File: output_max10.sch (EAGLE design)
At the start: 59 parts, among them IC4 IS61WV1288EEBLL-10HLI, IC5 10M04EQFP144, Q1 25MHz

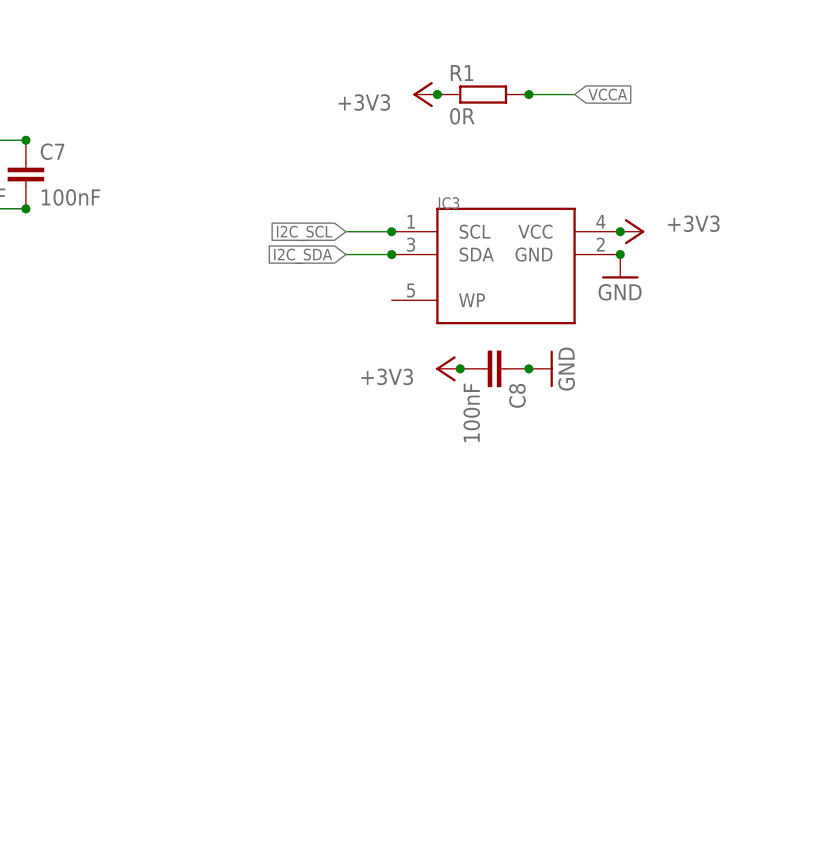
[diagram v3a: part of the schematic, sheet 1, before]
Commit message: clean up board some more; change eeprom to SOIC
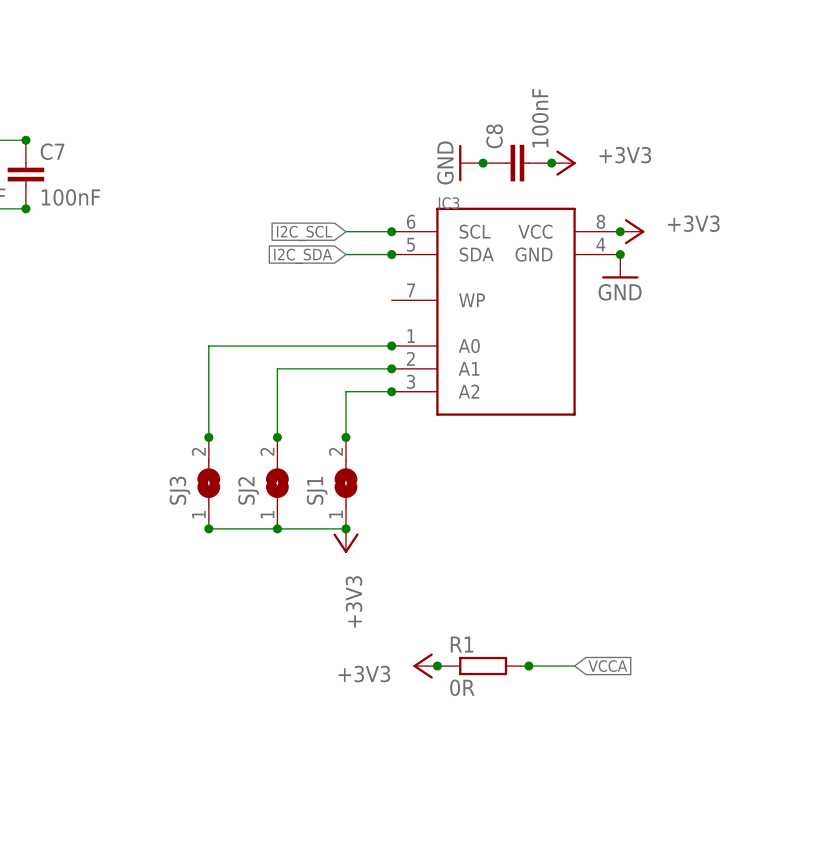
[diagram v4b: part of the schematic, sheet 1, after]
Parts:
- added SJ1, SJ2, SJ3: (no value), jumper:SJ
- IC3: device lichtenstein_onion:AT24C02D -> lichtenstein_onion:AT24C02DSOIC-8
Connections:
- new net N$5: IC3.A2, SJ1.2
- new net N$6: IC3.A1, SJ2.2
- new net N$7: IC3.A0, SJ3.2
- net +3V3: now also SJ1.1, SJ2.1, SJ3.1
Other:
- moved on the sheet: C8, R1
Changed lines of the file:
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@@
 <attribute name="MOUSER" value="710-885012207072"/>
 </part>
-<part name="IC3" library="lichtenstein_onion" deviceset="AT24C02D" device=""/>
 <part name="C8" library="rcl" library_urn="urn:adsk.eagle:library:334" deviceset="C-EU" device="C0805" package3d_urn="urn:adsk.eagle:package:23617/2" value="100nF">
 <attribute name="MOUSER" value="710-885012207072"/>
@@
 <part name="GND23" library="supply1" library_urn="urn:adsk.eagle:library:371" deviceset="GND" device=""/>
 <part name="+3V6" library="supply1" library_urn="urn:adsk.eagle:library:371" deviceset="+3V3" device=""/>
+<part name="IC3" library="lichtenstein_onion" deviceset="AT24C02D" device="SOIC-8"/>
+<part name="SJ1" library="jumper" library_urn="urn:adsk.eagle:library:252" deviceset="SJ" device="" package3d_urn="urn:adsk.eagle:package:15471/1"/>
+<part name="SJ2" library="jumper" library_urn="urn:adsk.eagle:library:252" deviceset="SJ" device="" package3d_urn="urn:adsk.eagle:package:15471/1"/>
+<part name="SJ3" library="jumper" library_urn="urn:adsk.eagle:library:252" deviceset="SJ" device="" package3d_urn="urn:adsk.eagle:package:15471/1"/>
+<part name="+3V7" library="supply1" library_urn="urn:adsk.eagle:library:371" deviceset="+3V3" device=""/>
 </parts>
 <sheets>
@@
 <attribute name="MOUSER" x="53.34" y="167.64" size="1.27" layer="96" display="off"/>
 </instance>
-<instance part="R1" gate="G$1" x="114.3" y="175.26">
-<attribute name="MOUSER" x="114.3" y="175.26" size="1.27" layer="96" align="top-center" display="off"/>
-</instance>
-<instance part="+3V36" gate="G$1" x="106.68" y="175.26" smashed="yes" rot="R90">
-<attribute name="VALUE" x="104.14" y="175.26" size="1.778" layer="96" rot="R180"/>
-</instance>
-<instance part="IC3" gate="G$1" x="109.22" y="162.56"/>
-<instance part="C8" gate="G$1" x="116.84" y="144.78" rot="R270">
-<attribute name="MOUSER" x="116.84" y="144.78" size="1.27" layer="96" rot="R270" align="top-center" display="off"/>
-</instance>
-<instance part="GND9" gate="1" x="121.92" y="144.78" rot="R90"/>
-<instance part="+3V37" gate="G$1" x="109.22" y="144.78" smashed="yes" rot="R90">
-<attribute name="VALUE" x="106.68" y="144.78" size="1.778" layer="96" rot="R180"/>
+<instance part="R1" gate="G$1" x="114.3" y="111.76">
+<attribute name="MOUSER" x="114.3" y="111.76" size="1.27" layer="96" align="top-center" display="off"/>
+</instance>
+<instance part="+3V36" gate="G$1" x="106.68" y="111.76" smashed="yes" rot="R90">
+<attribute name="VALUE" x="104.14" y="111.76" size="1.778" layer="96" rot="R180"/>
+</instance>
+<instance part="C8" gate="G$1" x="116.84" y="167.64" rot="R90">
+<attribute name="MOUSER" x="116.84" y="167.64" size="1.27" layer="96" rot="R90" align="top-center" display="off"/>
+</instance>
+<instance part="GND9" gate="1" x="111.76" y="167.64" rot="R270"/>
+<instance part="+3V37" gate="G$1" x="124.46" y="167.64" smashed="yes" rot="R270">
+<attribute name="VALUE" x="127" y="167.64" size="1.778" layer="96"/>
 </instance>
 <instance part="+3V38" gate="G$1" x="132.08" y="160.02" smashed="yes" rot="R270">
@@
 <instance part="H3" gate="G$1" x="121.92" y="12.7"/>
 <instance part="H4" gate="G$1" x="121.92" y="5.08"/>
+<instance part="IC3" gate="G$1" x="109.22" y="162.56"/>
+<instance part="SJ1" gate="1" x="99.06" y="132.08" rot="R90"/>
+<instance part="SJ2" gate="1" x="91.44" y="132.08" rot="R90"/>
+<instance part="SJ3" gate="1" x="83.82" y="132.08" rot="R90"/>
+<instance part="+3V7" gate="G$1" x="99.06" y="124.46" smashed="yes" rot="R180">
+<attribute name="VALUE" x="99.06" y="121.92" size="1.778" layer="96" rot="R270"/>
+</instance>
 </instances>
 <busses>
@@
 <pinref part="R1" gate="G$1" pin="1"/>
 <pinref part="+3V36" gate="G$1" pin="+3V3"/>
-<junction x="109.22" y="175.26"/>
+<junction x="109.22" y="111.76"/>
 </segment>
 <segment>
 <pinref part="C8" gate="G$1" pin="2"/>
 <pinref part="+3V37" gate="G$1" pin="+3V3"/>
-<junction x="111.76" y="144.78"/>
-</segment>
-<segment>
+<junction x="121.92" y="167.64"/>
+</segment>
+<segment>
+<pinref part="+3V38" gate="G$1" pin="+3V3"/>
 <pinref part="IC3" gate="G$1" pin="VCC"/>
-<pinref part="+3V38" gate="G$1" pin="+3V3"/>
 <junction x="129.54" y="160.02"/>
+</segment>
+<segment>
+<pinref part="SJ3" gate="1" pin="1"/>
+<pinref part="SJ1" gate="1" pin="1"/>
+<wire x1="83.82" y1="127" x2="91.44" y2="127" width="0.1524" layer="91"/>
+<pinref part="+3V7" gate="G$1" pin="+3V3"/>
+<junction x="99.06" y="127"/>
+<pinref part="SJ2" gate="1" pin="1"/>
+<junction x="91.44" y="127"/>
+<wire x1="91.44" y1="127" x2="99.06" y2="127" width="0.1524" layer="91"/>
+<junction x="83.82" y="127"/>
 </segment>
 </net>
@@
 <pinref part="C8" gate="G$1" pin="1"/>
 <pinref part="GND9" gate="1" pin="GND"/>
-<junction x="119.38" y="144.78"/>
-</segment>
-<segment>
+<junction x="114.3" y="167.64"/>
+</segment>
+<segment>
+<pinref part="GND10" gate="1" pin="GND"/>
 <pinref part="IC3" gate="G$1" pin="GND"/>
-<pinref part="GND10" gate="1" pin="GND"/>
 <junction x="129.54" y="157.48"/>
 </segment>
@@
 </segment>
 <segment>
-<pinref part="IC3" gate="G$1" pin="SCL"/>
 <wire x1="104.14" y1="160.02" x2="99.06" y2="160.02" width="0.1524" layer="91"/>
 <label x="99.06" y="160.02" size="1.27" layer="95" rot="R180" xref="yes"/>
+<pinref part="IC3" gate="G$1" pin="SCL"/>
 <junction x="104.14" y="160.02"/>
 </segment>
@@
 </segment>
 <segment>
-<pinref part="IC3" gate="G$1" pin="SDA"/>
 <wire x1="104.14" y1="157.48" x2="99.06" y2="157.48" width="0.1524" layer="91"/>
 <label x="99.06" y="157.48" size="1.27" layer="95" rot="R180" xref="yes"/>
+<pinref part="IC3" gate="G$1" pin="SDA"/>
 <junction x="104.14" y="157.48"/>
 </segment>
@@
 <segment>
 <pinref part="R1" gate="G$1" pin="2"/>
-<wire x1="119.38" y1="175.26" x2="124.46" y2="175.26" width="0.1524" layer="91"/>
-<label x="124.46" y="175.26" size="1.27" layer="95" xref="yes"/>
-<junction x="119.38" y="175.26"/>
+<wire x1="119.38" y1="111.76" x2="124.46" y2="111.76" width="0.1524" layer="91"/>
+<label x="124.46" y="111.76" size="1.27" layer="95" xref="yes"/>
+<junction x="119.38" y="111.76"/>
 </segment>
 </net>
@@
 </segment>
 </net>
+<net name="N$5" class="0">
+<segment>
+<pinref part="SJ1" gate="1" pin="2"/>
+<pinref part="IC3" gate="G$1" pin="A2"/>
+<wire x1="99.06" y1="137.16" x2="99.06" y2="142.24" width="0.1524" layer="91"/>
+<wire x1="99.06" y1="142.24" x2="104.14" y2="142.24" width="0.1524" layer="91"/>
+<junction x="99.06" y="137.16"/>
+<junction x="104.14" y="142.24"/>
+</segment>
+</net>
+<net name="N$6" class="0">
+<segment>
+<pinref part="IC3" gate="G$1" pin="A1"/>
+<pinref part="SJ2" gate="1" pin="2"/>
+<wire x1="104.14" y1="144.78" x2="91.44" y2="144.78" width="0.1524" layer="91"/>
+<wire x1="91.44" y1="144.78" x2="91.44" y2="137.16" width="0.1524" layer="91"/>
+<junction x="91.44" y="137.16"/>
+<junction x="104.14" y="144.78"/>
+</segment>
+</net>
+<net name="N$7" class="0">
+<segment>
+<pinref part="SJ3" gate="1" pin="2"/>
+<pinref part="IC3" gate="G$1" pin="A0"/>
+<wire x1="83.82" y1="137.16" x2="83.82" y2="147.32" width="0.1524" layer="91"/>
+<wire x1="83.82" y1="147.32" x2="104.14" y2="147.32" width="0.1524" layer="91"/>
+<junction x="83.82" y="137.16"/>
+<junction x="104.14" y="147.32"/>
+</segment>
+</net>

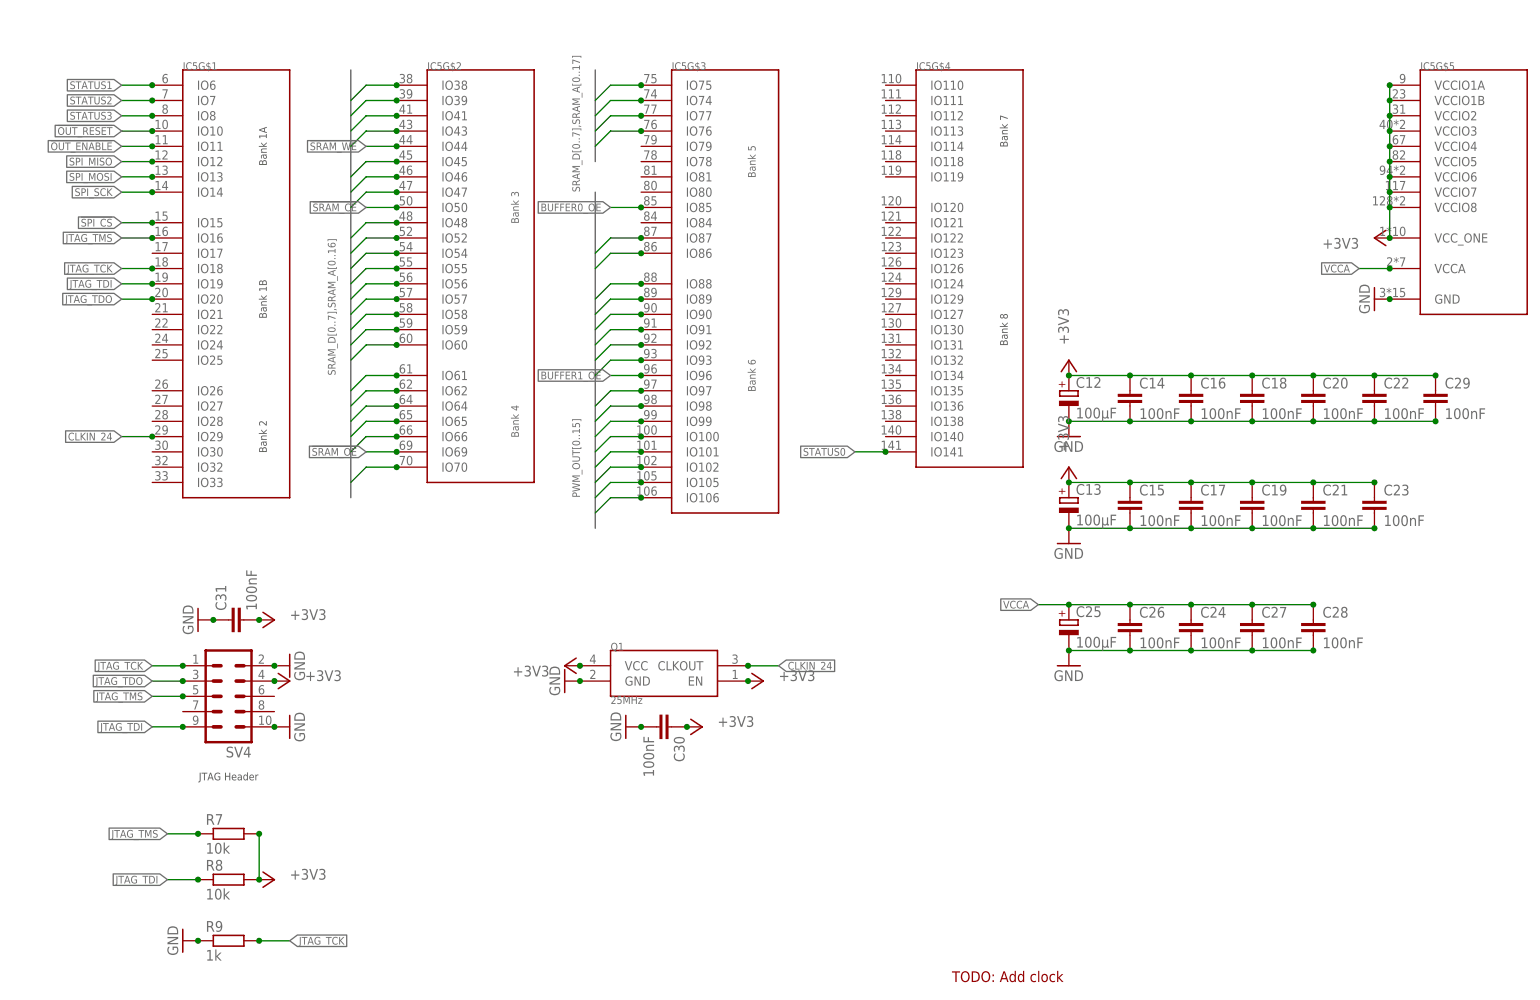
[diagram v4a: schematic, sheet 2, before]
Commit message: Fixed bulk capacitor footprints; made +V for output channels independent on output board
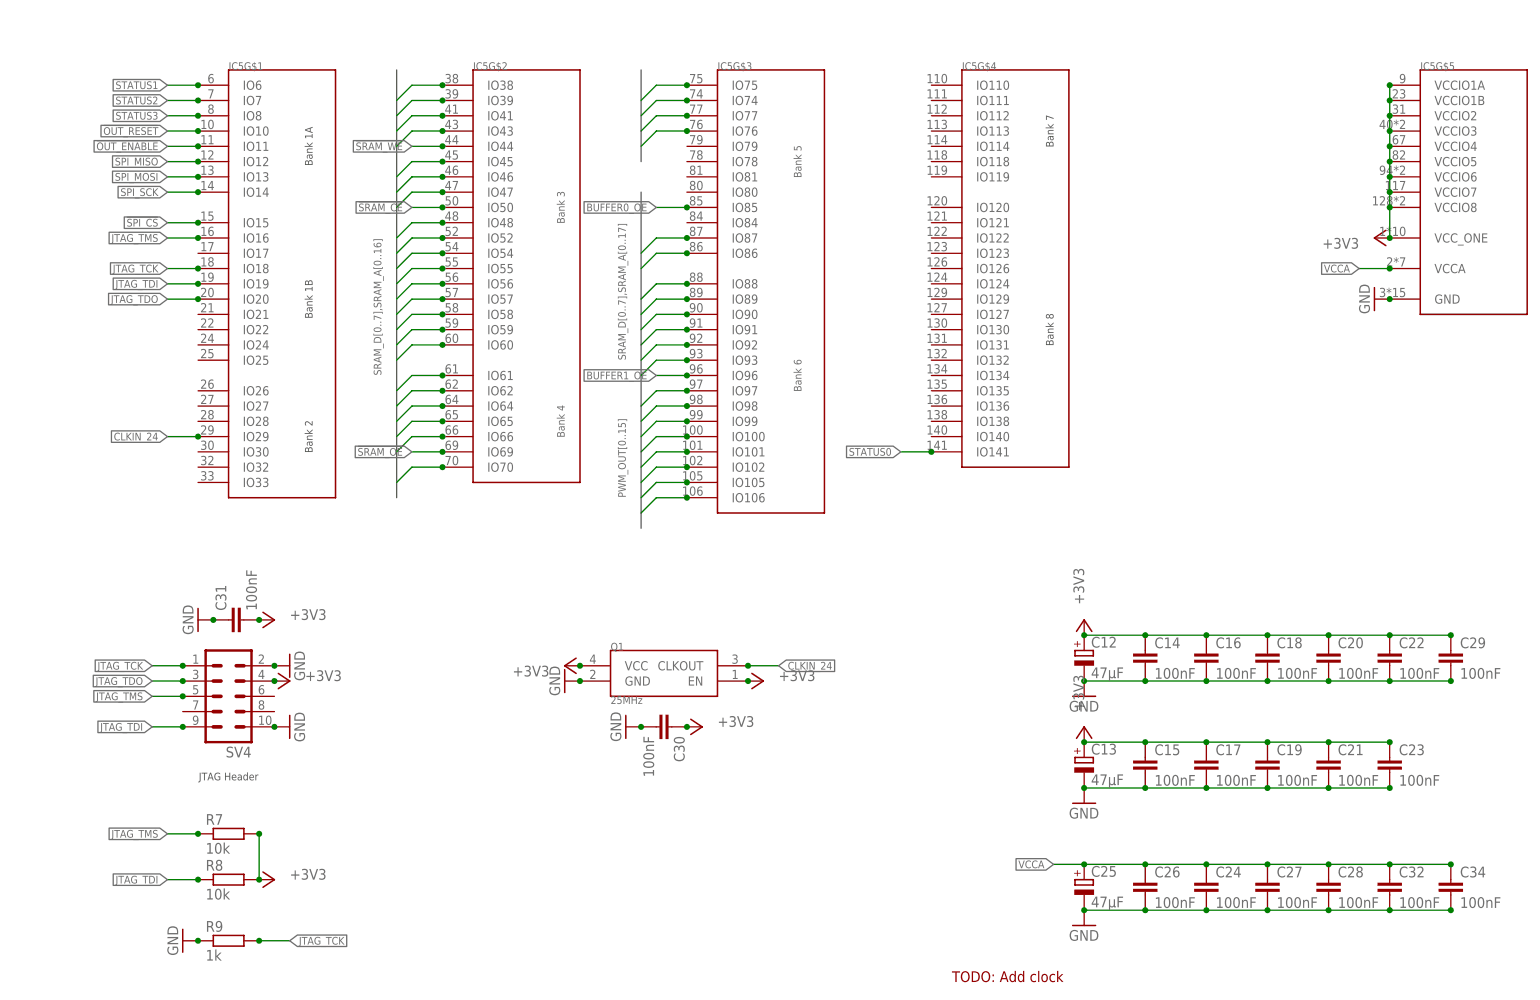
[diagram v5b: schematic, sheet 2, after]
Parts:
- added C32, C33, C34: 100nF, rcl:C-EUC0805
- added SV5: (no value), con-lstb:MA05-2
- C12, C13, C25, C4, C9: value 100µF -> 47µF; device rcl:CPOL-EUSMCD -> rcl:CPOL-EUCT7343; MOUSER 581-NOSD107M006 -> 581-TAJD476M016RNJV
- C6: device rcl:CPOL-EUSMCD -> rcl:CPOL-EUCT7343
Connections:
- removed net V+: C3.1, C5.1, IC1.VCCB, IC2.VCCB, SV2.2, SV3.2
- new net V+0: C5.1, IC1.VCCB, SV2.2
- new net V+1: C3.1, IC2.VCCB, SV3.2
- net +3V3: now also C33.1, SV5.2, SV5.4
- net GND: now also C32.2, C33.2, C34.2, SV5.1, SV5.3
- net I2C_SCL: now also SV5.10
- net I2C_SDA: now also SV5.8
- net VCCA: now also C32.1, C34.1
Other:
- note added: "Address jumpers: changes low 3 bits of EEPROM address. Should be open by default"
- note added: "Front Panel Connector"
- moved on the sheet: C1, C12, C13, C14, C15, C16, C17, C18, C19, C2, C20, C21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
